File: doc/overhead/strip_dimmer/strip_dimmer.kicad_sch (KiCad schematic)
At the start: 9 parts, among them J1 SERIAL_OUT, J2 POWER_IN, J4 POWER_OUT, J5 LED_STRIP, J6 SERIAL_IN, Q1 IRLB8721PBF, Q2 IRLB8721PBF, U1 ATtiny85-20S, U2 TPS70933DBVR

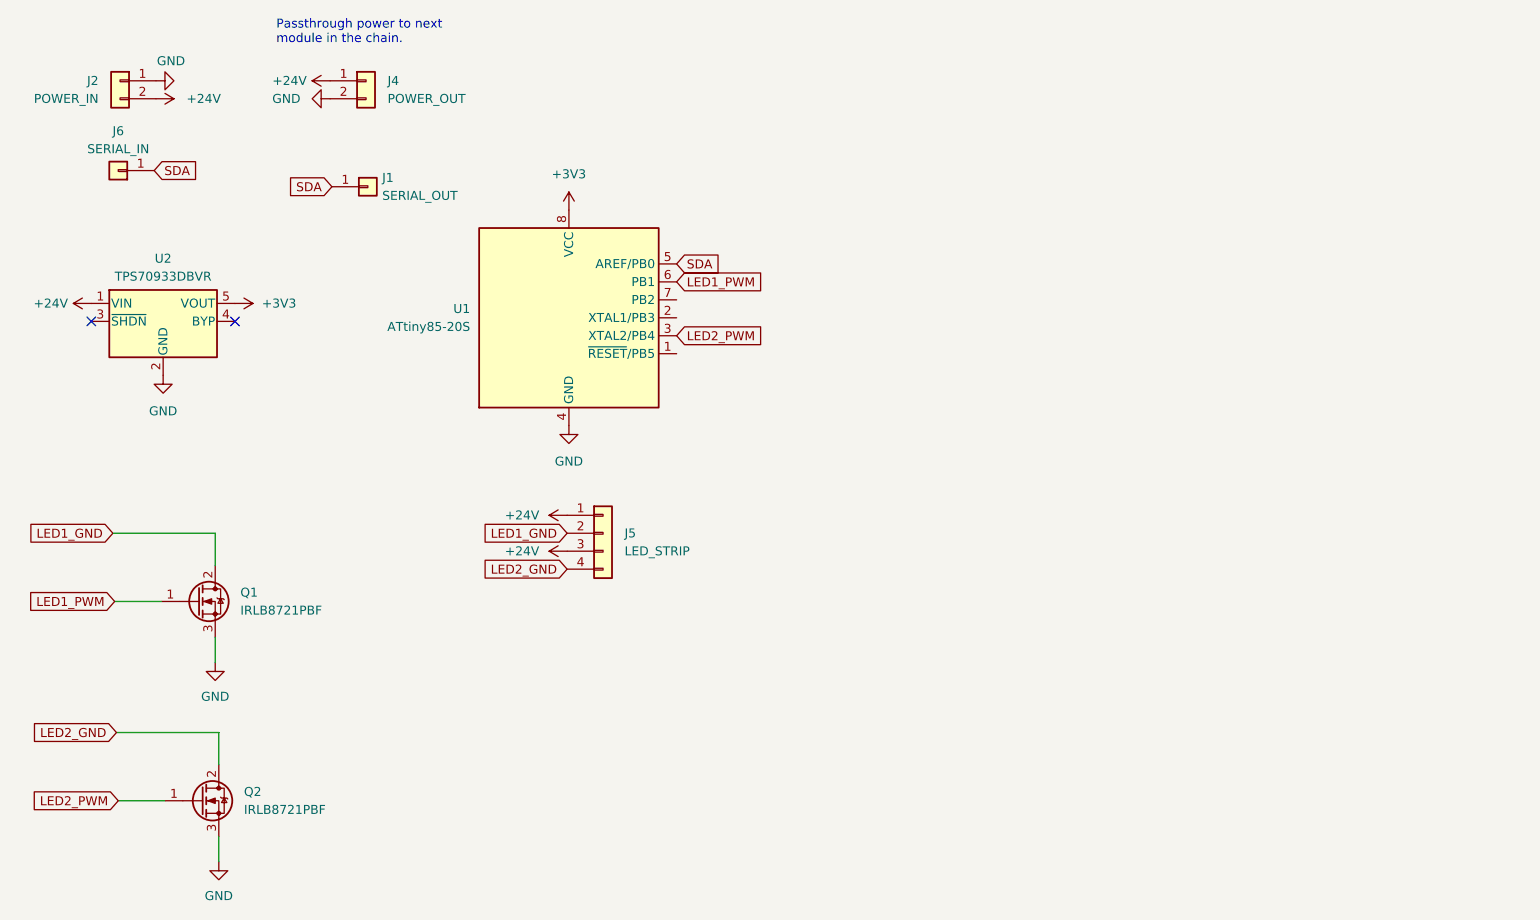
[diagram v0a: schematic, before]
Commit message: Add PCB CAM and Voron toolboard stuff.
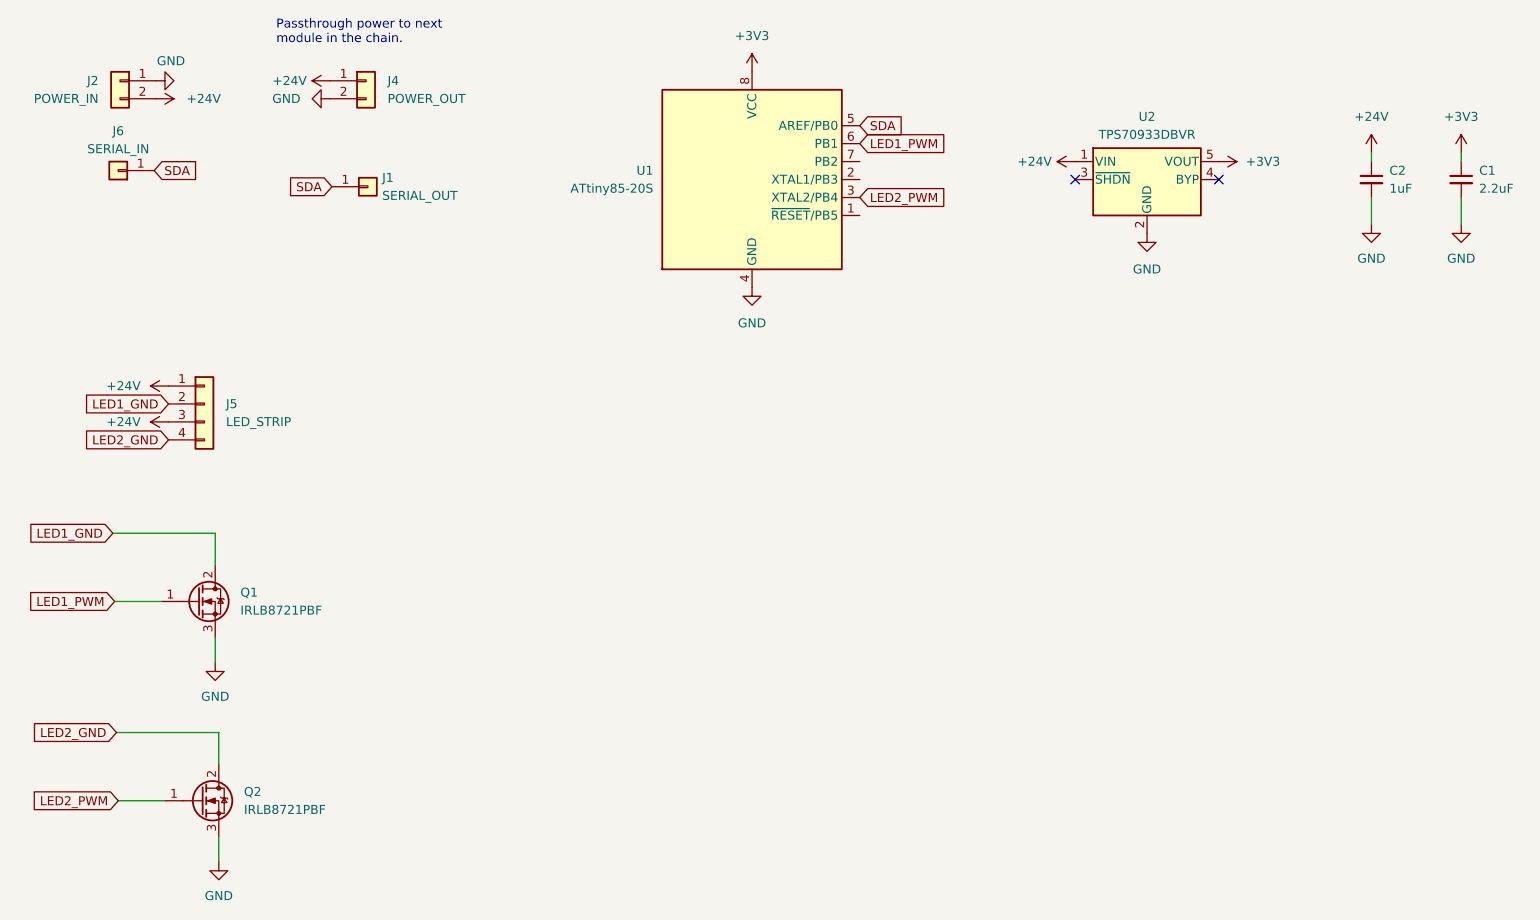
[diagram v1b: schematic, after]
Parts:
- added C1: 2.2uF, Capacitor_SMD:C_0805_2012Metric_Pad1.18x1.45mm_HandSolder, symbol Device:C_Small
- added C2: 1uF, Capacitor_SMD:C_0805_2012Metric_Pad1.18x1.45mm_HandSolder, symbol Device:C_Small
- U2: footprint Package_TO_SOT_SMD:SOT-353_SC-70-5 -> Package_TO_SOT_SMD:SOT-23-5_HandSoldering
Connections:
- net +24V: now also C2.1
- net +3V3: now also C1.1
- net GND: now also C1.2, C2.2
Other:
- moved on the sheet: J5, U1, U2
